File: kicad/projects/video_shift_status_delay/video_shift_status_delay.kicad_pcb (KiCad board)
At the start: 2 copper layers, 203.2 x 97.8 mm, 54 parts, among them J1 peripheral_addr_bus_connector, J10 ENABLE DELAY, J2 peripheral_aux_connector, J3 peripheral_membank_connector, J4 Conn_01x16_Socket, J5 Conn_01x16_Socket, J6 video_aux, J7 Conn_01x03_Pin, J8 Conn_01x04_Socket, J9 Conn_02x06_Odd_Even, U1 74HC245, U10 74HC377, U11 74HC138, U12 74HC04, U13 74HC10, U14 74HC04, U15 74HC08, U2 74HC245, U3 74HC245, U4 74HC245, U5 74HC245, U6 74HC245, U7 74HC245, U8 74HC245, U9 74HC245

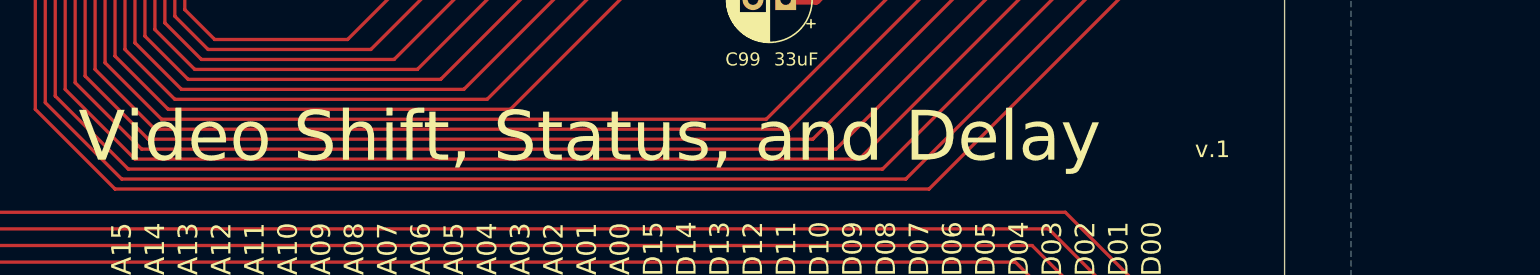
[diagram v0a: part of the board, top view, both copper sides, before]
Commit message: Last few tech checks - gnd test points and video cursor/scan input switch order for vid output left to check.
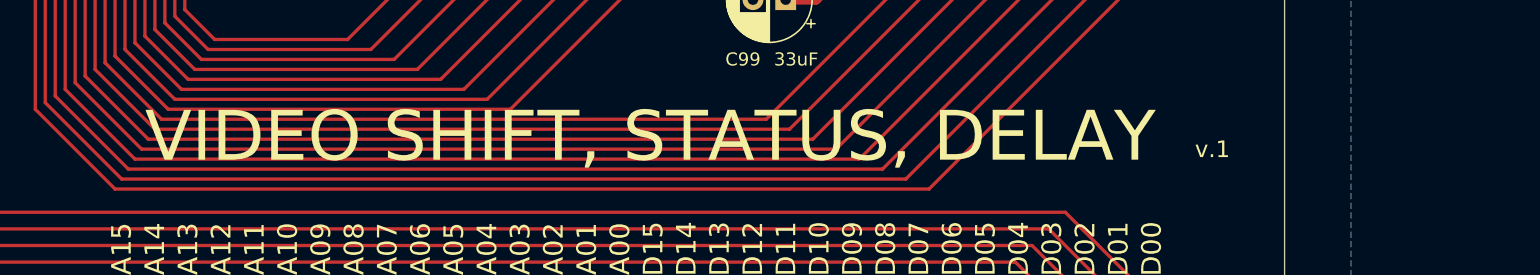
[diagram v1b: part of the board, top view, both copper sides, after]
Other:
- board text added: "VIDEO SHIFT, STATUS, DELAY"
- board text removed: "Video Shift, Status, and Delay"
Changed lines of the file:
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@@
     (effects (font (size 1.27 1.27) (thickness 0.2032)) (justify left bottom))
   )
-  (gr_text "Video Shift, Status, and Delay" (at 161.798 134.62) (layer "F.SilkS")
+  (gr_text "VIDEO SHIFT, STATUS, DELAY" (at 166.878 134.62) (layer "F.SilkS")
     (effects (font (size 3.81 3.81) (thickness 0.381)) (justify left bottom))
   )

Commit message: I think all the latest set of boards is done...
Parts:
- removed RN1: 10K, Resistor_THT:R_Array_SIP9
- added C16: 0.1uF, Capacitor_THT:C_Disc_D5.0mm_W2.5mm_P5.00mm, F.Cu at (61.0, 124.5)
- added U16: 74HC161, Package_DIP:DIP-16_W7.62mm_Socket, F.Cu at (66.0, 132.1)
- C1, C10, C11, C12, C13, C14, C15, C2, C3, C4, C5, C6, C7, C8, C9: value C -> 0.1uF
- moved C98 23.1 mm to (56.1, 139.1)
- moved C97 14.7 mm to (113.8, 81.3)
- moved R7 0.25 mm to (106.7, 110.2)
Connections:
- J1 pad 6: unconnected-(J1-D_05-Pad6) -> /DATA_BUS_05
- J1 pad 7: unconnected-(J1-D_06-Pad7) -> /DATA_BUS_06
- J1 pad 8: unconnected-(J1-D_07-Pad8) -> /DATA_BUS_07
- U10 pad 12: unconnected-(U10-Q4-Pad12) -> /SHIFT_SEL_1
- U10 pad 13: GND -> /DATA_BUS_04
- U10 pad 14: GND -> /DATA_BUS_05
- U10 pad 15: unconnected-(U10-Q5-Pad15) -> /BANK_SEL
- U10 pad 2: /BANK_SEL -> unconnected-(U10-Q0-Pad2)
- U10 pad 3: /DATA_BUS_02 -> GND
- U10 pad 4: /DATA_BUS_01 -> GND
- U10 pad 5: /SHIFT_SEL_1 -> unconnected-(U10-Q1-Pad5)
- U10 pad 6: /SHIFT_SEL_0 -> unconnected-(U10-Q2-Pad6)
- U10 pad 7: /DATA_BUS_00 -> GND
- U10 pad 8: GND -> /DATA_BUS_03
- U10 pad 9: unconnected-(U10-Q3-Pad9) -> /SHIFT_SEL_0
- U12 pad 3: GND -> /V_BLANK
- U12 pad 4: unconnected-(U12-Pad4) -> Net-(U16-CP)
- U9 pad 11: /SHIFT_SEL_0 -> /V_BLANK
- U9 pad 12: /SHIFT_SEL_1 -> /H_BLANK
- U9 pad 14: /H_BLANK -> /SHIFT_SEL_1
- U9 pad 15: /V_BLANK -> /SHIFT_SEL_0
- U9 pad 16: Net-(RN1-R4) -> /FRAME_COUNT_2
- U9 pad 17: Net-(RN1-R5) -> /FRAME_COUNT_1
- U9 pad 18: Net-(RN1-R6) -> /FRAME_COUNT_0
- U9 pad 2: Net-(RN1-R1) -> /DATA_BUS_00
- U9 pad 3: Net-(RN1-R2) -> /DATA_BUS_01
- U9 pad 4: Net-(RN1-R3) -> /DATA_BUS_02
- U9 pad 5: /DATA_BUS_04 -> /DATA_BUS_03
- U9 pad 6: /DATA_BUS_03 -> /DATA_BUS_04
- U9 pad 7: /DATA_BUS_02 -> /DATA_BUS_05
- U9 pad 8: /DATA_BUS_01 -> /DATA_BUS_06
- U9 pad 9: /DATA_BUS_00 -> /DATA_BUS_07
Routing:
- net /DATA_BUS_05: track 0.00 -> 184.6 mm, vias 0 -> 2
- net /DATA_BUS_06: track 0.00 -> 159.0 mm, vias 0 -> 2
- net /DATA_BUS_07: track 0.00 -> 155.0 mm
- net /V_BLANK: track 78.1 -> 164.6 mm, vias 1 -> 6
- net Net-(U16-CP): track 0.00 -> 76.7 mm, vias 0 -> 6
- net VCC: track 564.4 -> 610.8 mm, vias 15 -> 17
- net Net-(RN1-R6): track 29.9 -> 0.00 mm
- net /DATA_BUS_02: track 213.2 -> 184.2 mm, vias 2 -> 3
- net /DATA_BUS_04: track 180.6 -> 208.0 mm, vias 0 -> 2
- net Net-(RN1-R5): track 24.2 -> 0.00 mm
- net /DATA_BUS_03: track 179.4 -> 203.6 mm
- net /DATA_BUS_01: track 210.8 -> 190.1 mm, vias 4 -> 3
- net /BANK_SEL: track 188.2 -> 171.4 mm
- net Net-(RN1-R4): track 16.3 -> 0.00 mm
- net /FRAME_COUNT_0: track 0.00 -> 13.8 mm
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
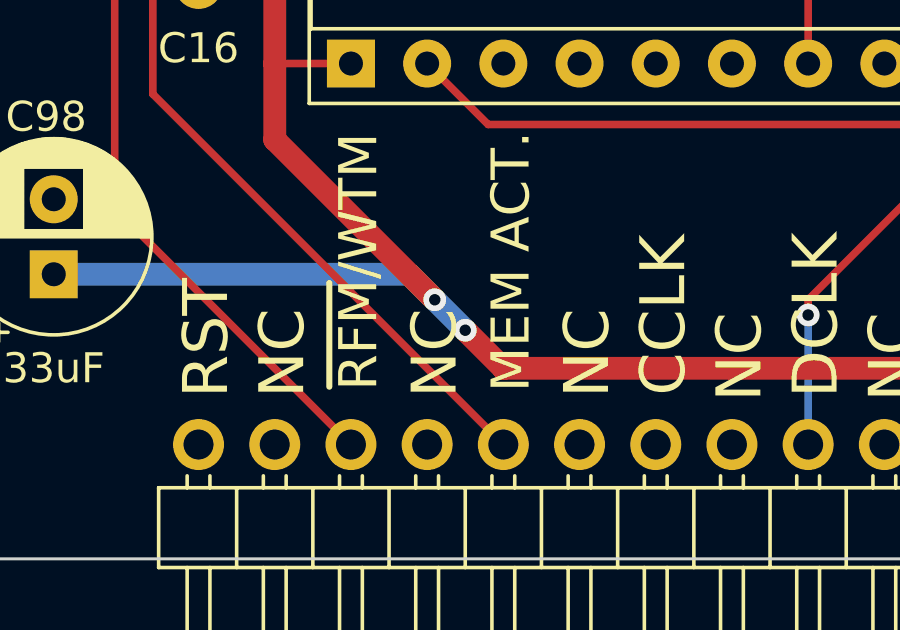
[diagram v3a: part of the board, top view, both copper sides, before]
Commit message: Fix missing section of VCC track on vid shift status delay.
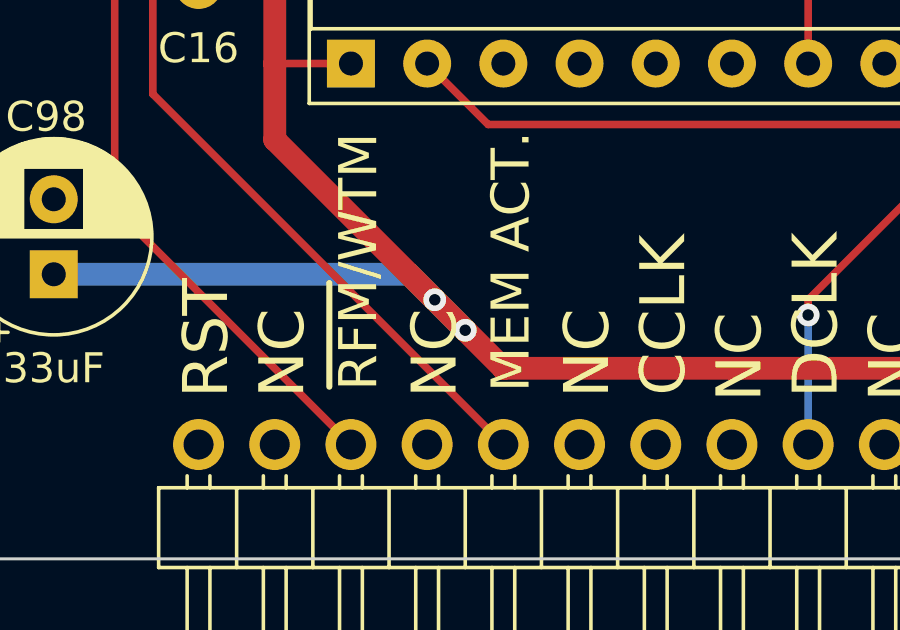
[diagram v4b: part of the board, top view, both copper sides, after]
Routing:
- net VCC: track 610.8 -> 612.3 mm
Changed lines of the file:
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@@
   (segment (start 66.04 88.392) (end 84.328 88.392) (width 0.762) (layer "F.Cu") (net 1))
   (segment (start 180.34 68.834) (end 166.116 68.834) (width 0.762) (layer "F.Cu") (net 1))
+  (segment (start 68.834 139.954) (end 69.85 140.97) (width 0.762) (layer "F.Cu") (net 1))
   (segment (start 68.072 97.028) (end 66.04 99.06) (width 0.254) (layer "F.Cu") (net 1))
   (segment (start 180.26 73.66) (end 182.88 73.66) (width 0.254) (layer "F.Cu") (net 1))
